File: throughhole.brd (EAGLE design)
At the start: 40.3 x 35.5 mm, 4 parts, among them J1 2.1MMJACKTHM

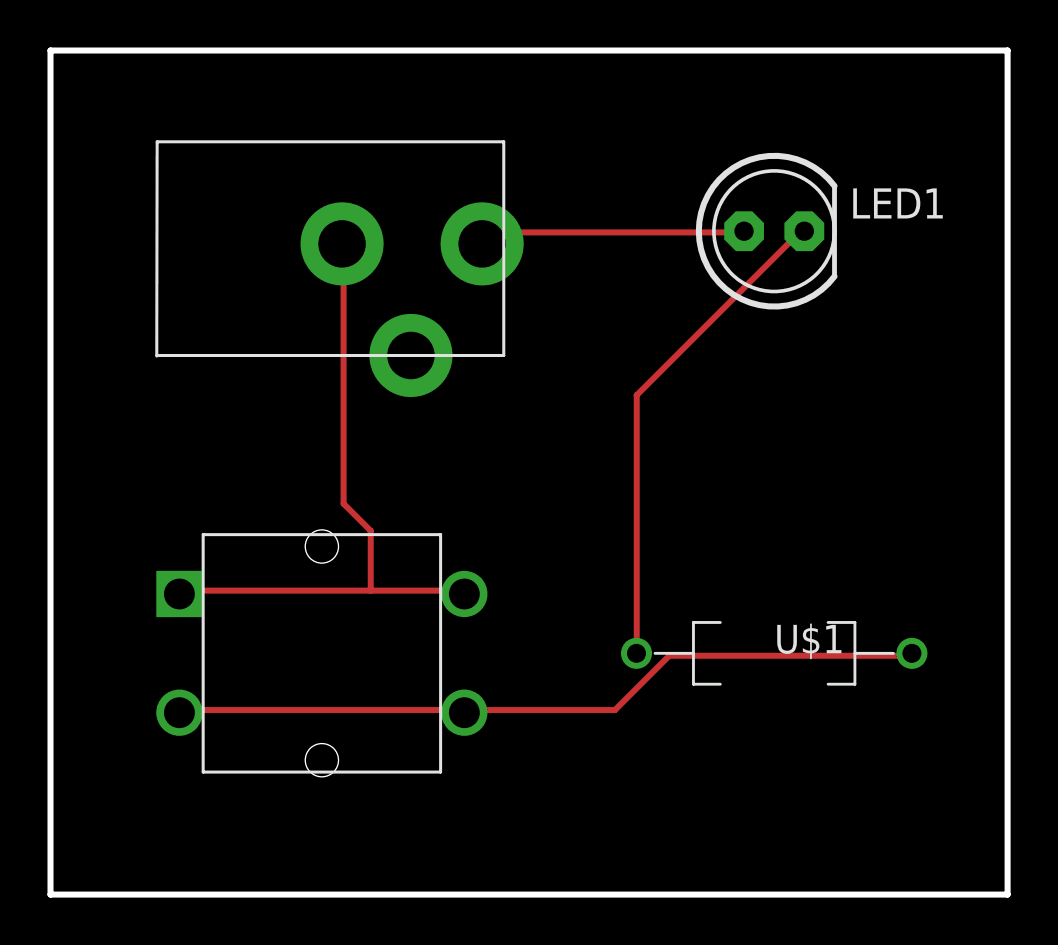
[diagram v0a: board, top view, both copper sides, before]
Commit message: Added logo to the boards.
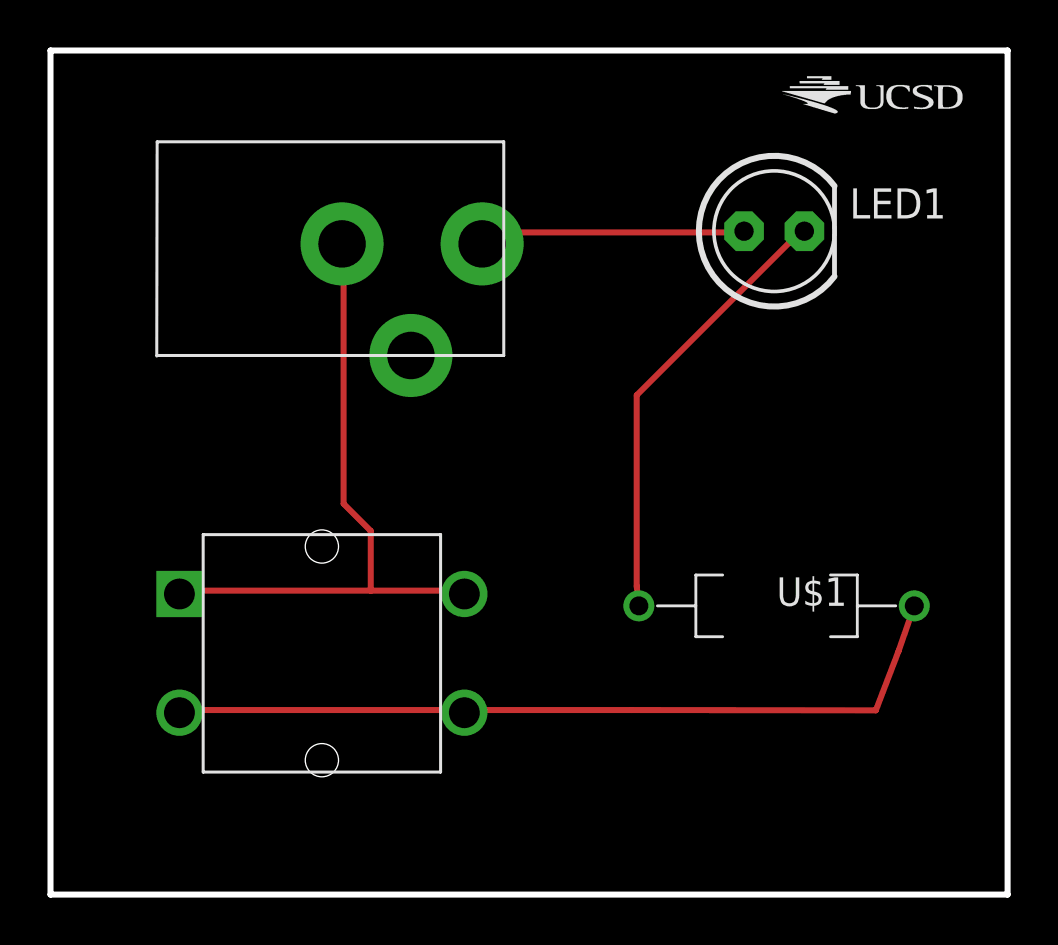
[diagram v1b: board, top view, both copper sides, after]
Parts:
- added U$2: (no value), Logos:UCSD_LOGO
- moved U$1 2.00 mm to (30.6, 12.2)
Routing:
- net N$3: track 32.0 -> 34.2 mm
- net N$2: track 20.8 -> 18.8 mm
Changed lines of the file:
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@@
 <element name="LED1" library="Lab2" package="LED5MM" value="Red" x="30.48" y="27.94"/>
 <element name="S1" library="Lab2" package="BUTTON-TACTILE-SQUARE-ADAFRUIT1010" value="BUTTON-TACTILE-SQUARE" x="11.43" y="10.16"/>
-<element name="U$1" library="Lab2" package="RESAD1160W55L680D260_HS" value="330Ohms" x="30.48" y="10.16">
-<attribute name="DIST1" value="" x="30.48" y="10.16" size="1.778" layer="27" display="off"/>
-<attribute name="CASE" value="" x="30.48" y="10.16" size="1.778" layer="27" display="off"/>
-<attribute name="DIST1PN" value="" x="30.48" y="10.16" size="1.778" layer="27" display="off"/>
-<attribute name="MFR" value="" x="30.48" y="10.16" size="1.778" layer="27" display="off"/>
-<attribute name="MPN" value="" x="30.48" y="10.16" size="1.778" layer="27" display="off"/>
-<attribute name="VAL" value="" x="30.48" y="10.16" size="1.778" layer="27" display="off"/>
-<attribute name="DESC" value="" x="30.48" y="10.16" size="1.778" layer="27" display="off"/>
-<attribute name="SIZE" value="" x="30.48" y="10.16" size="1.778" layer="27" display="off"/>
-<attribute name="PWR" value="" x="30.48" y="10.16" size="1.778" layer="27" display="off"/>
-<attribute name="TOL" value="" x="30.48" y="10.16" size="1.778" layer="27" display="off"/>
-<attribute name="URL" value="" x="30.48" y="10.16" size="1.778" layer="27" display="off"/>
+<element name="U$1" library="Lab2" package="RESAD1160W55L680D260_HS" value="330Ohms" x="30.58" y="12.16">
+<attribute name="DIST1" value="" x="30.58" y="12.16" size="1.778" layer="27" display="off"/>
+<attribute name="CASE" value="" x="30.58" y="12.16" size="1.778" layer="27" display="off"/>
+<attribute name="DIST1PN" value="" x="30.58" y="12.16" size="1.778" layer="27" display="off"/>
+<attribute name="MFR" value="" x="30.58" y="12.16" size="1.778" layer="27" display="off"/>
+<attribute name="MPN" value="" x="30.58" y="12.16" size="1.778" layer="27" display="off"/>
+<attribute name="VAL" value="" x="30.58" y="12.16" size="1.778" layer="27" display="off"/>
+<attribute name="DESC" value="" x="30.58" y="12.16" size="1.778" layer="27" display="off"/>
+<attribute name="SIZE" value="" x="30.58" y="12.16" size="1.778" layer="27" display="off"/>
+<attribute name="PWR" value="" x="30.58" y="12.16" size="1.778" layer="27" display="off"/>
+<attribute name="TOL" value="" x="30.58" y="12.16" size="1.778" layer="27" display="off"/>
+<attribute name="URL" value="" x="30.58" y="12.16" size="1.778" layer="27" display="off"/>
 </element>
+<element name="U$2" library="Logos" package="UCSD_LOGO" value="" x="30.8" y="32.9"/>
 </elements>
 <signals>
@@
 <contactref element="LED1" pad="K"/>
 <contactref element="U$1" pad="1"/>
-<wire x1="24.6888" y1="21.0312" x2="24.6888" y2="10.287" width="0.254" layer="1"/>
+<wire x1="24.6888" y1="21.0312" x2="24.6888" y2="12.987" width="0.254" layer="1"/>
 <wire x1="31.5468" y1="27.8892" x2="24.6888" y2="21.0312" width="0.254" layer="1"/>
-<wire x1="24.6888" y1="10.287" x2="24.68" y2="10.16" width="0.254" layer="1"/>
+<wire x1="24.6888" y1="12.987" x2="24.78" y2="12.16" width="0.254" layer="1"/>
 <wire x1="31.5468" y1="27.8892" x2="31.75" y2="27.94" width="0.254" layer="1"/>
 </signal>
@@
 <contactref element="U$1" pad="2"/>
 <contactref element="S1" pad="S"/>
-<wire x1="26.0604" y1="10.0584" x2="36.1188" y2="10.0584" width="0.254" layer="1"/>
-<wire x1="23.7744" y1="7.7724" x2="26.0604" y2="10.0584" width="0.254" layer="1"/>
-<wire x1="17.6022" y1="7.7724" x2="23.7744" y2="7.7724" width="0.254" layer="1"/>
-<wire x1="36.1188" y1="10.0584" x2="36.28" y2="10.16" width="0.254" layer="1"/>
+<wire x1="34.7604" y1="7.7584" x2="35.7188" y2="10.2584" width="0.254" layer="1"/>
+<wire x1="24.4744" y1="7.7724" x2="34.7604" y2="7.7584" width="0.254" layer="1"/>
+<wire x1="17.6022" y1="7.7724" x2="24.4744" y2="7.7724" width="0.254" layer="1"/>
+<wire x1="35.7188" y1="10.2584" x2="36.38" y2="12.16" width="0.254" layer="1"/>
 <wire x1="17.6022" y1="7.7724" x2="17.43" y2="7.66" width="0.254" layer="1"/>
 <wire x1="17.3736" y1="7.7724" x2="5.4864" y2="7.7724" width="0.254" layer="1"/>
